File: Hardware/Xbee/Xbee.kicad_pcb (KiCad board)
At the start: 2 copper layers, 100 x 50 mm, 44 parts, among them J1 Alimentación, J2 Raspberry, J3 Pines 1, J4 Pines 2, J5 Programación, J6 Entrada, J7 Salida, K1 Rele12V, Q1 BC338, Q2 BC338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

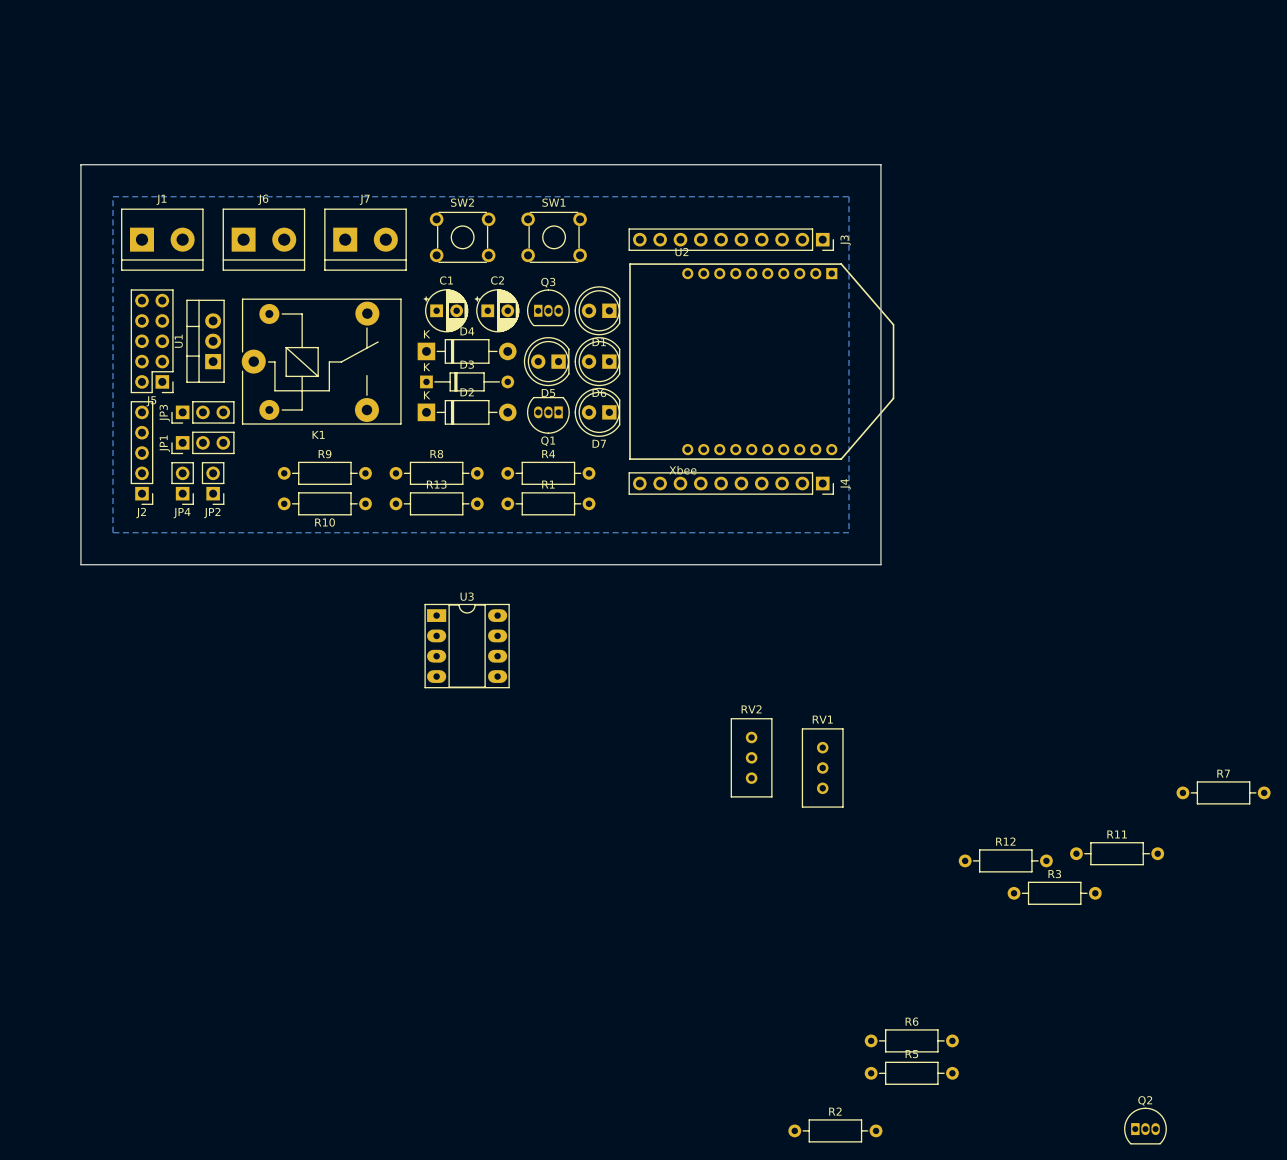
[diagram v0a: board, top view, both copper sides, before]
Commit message: PCB footprint placement
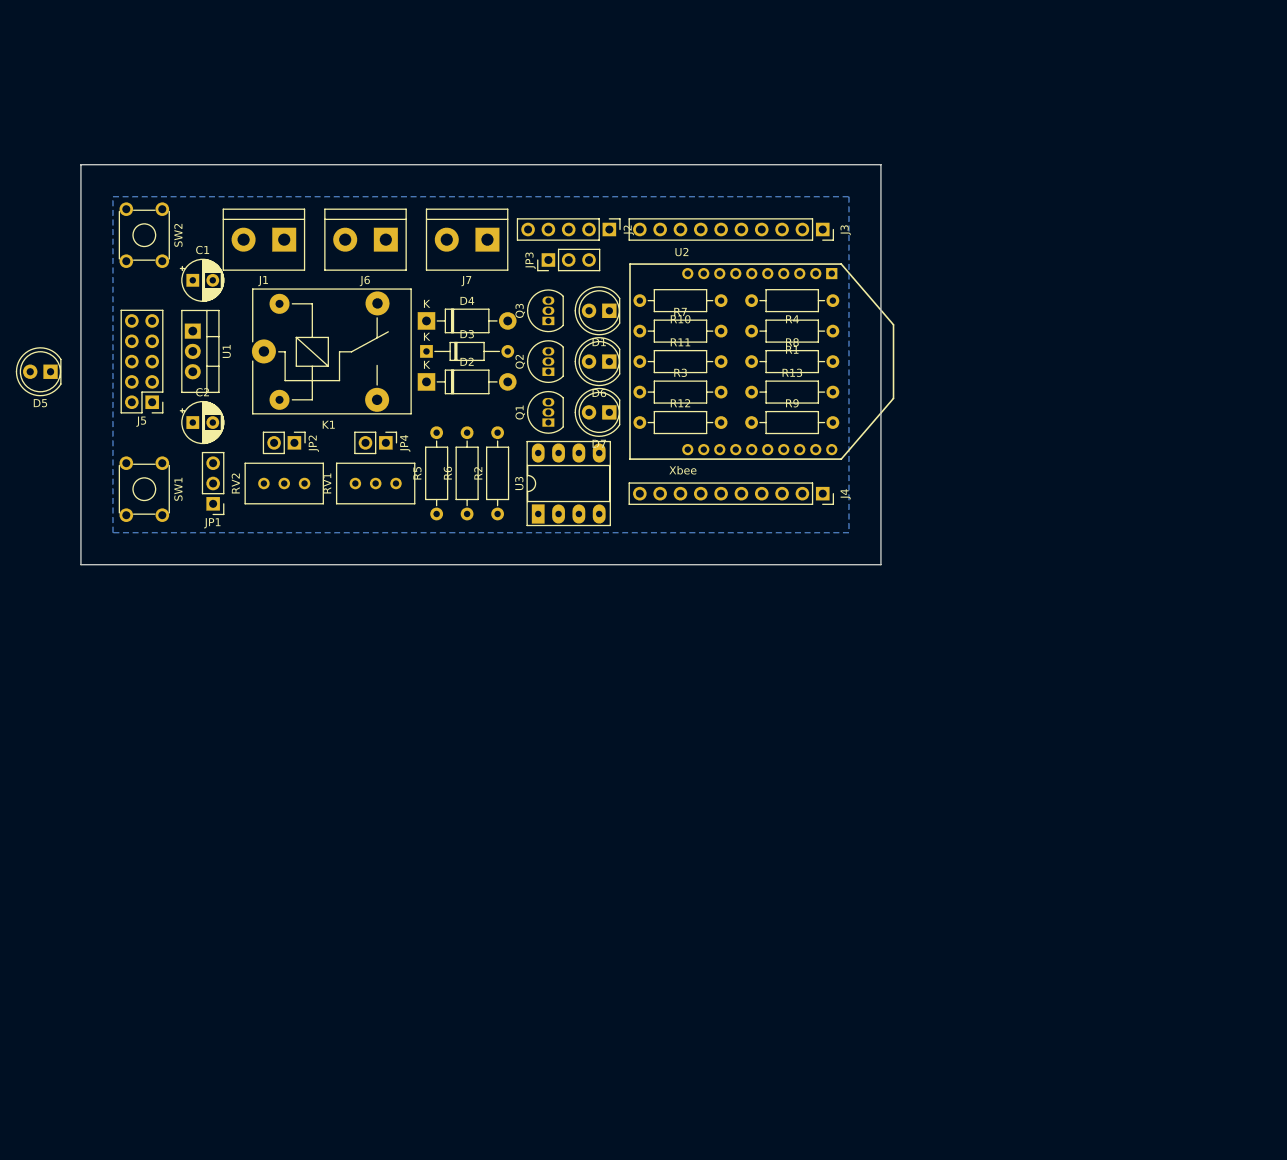
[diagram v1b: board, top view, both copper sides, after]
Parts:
- moved Q2 119.8 mm to (138.4, 55.9), turned to 90 degrees
- moved R7 89.1 mm to (149.9, 50.8)
- moved R5 88.5 mm to (124.5, 73.7), turned to 90 degrees
- moved R2 85.6 mm to (132.1, 73.7), turned to 90 degrees
- moved R6 83.0 mm to (128.3, 73.7), turned to 90 degrees
- moved R11 82.2 mm to (149.9, 54.6)
- moved R3 78.2 mm to (149.9, 58.4)
- moved RV2 68.7 mm to (102.9, 69.8), turned to 90 degrees
- moved R12 68.2 mm to (149.9, 62.2)
- moved J2 67.1 mm to (146.1, 38.1), turned to 270 degrees
- moved RV1 67.1 mm to (114.3, 69.8), turned to 90 degrees
- moved D5 63.5 mm to (76.2, 55.9)
- moved R9 58.8 mm to (163.8, 62.2)
- moved SW1 54.9 mm to (90.2, 67.3), turned to 270 degrees
- moved R10 51.2 mm to (160.0, 47.0)
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
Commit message: Started routing
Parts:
- added REF**: MountingHole_2.1mm, MountingHole:MountingHole_2.1mm, F.Cu at (177.5, 77.5)
- added REF**: MountingHole_2.1mm, MountingHole:MountingHole_2.1mm, F.Cu at (82.5, 77.5)
- added REF**: MountingHole_2.1mm, MountingHole:MountingHole_2.1mm, F.Cu at (177.5, 32.5)
- added REF**: MountingHole_2.1mm, MountingHole:MountingHole_2.1mm, F.Cu at (82.5, 32.5)
- D5, D6: footprint LED_THT:LED_D5.0mm -> Connector_PinSocket_2.54mm:PinSocket_1x02_P2.54mm_Vertical
- moved D5 63.6 mm to (138.4, 42.5), turned to 270 degrees
- moved JP3 41.1 mm to (106.7, 67.9), turned to 270 degrees
- moved D3 19.8 mm to (136.5, 67.9)
- moved U3 19.4 mm to (124.5, 59.1)
- moved RV2 15.3 mm to (118.1, 71.1), turned to 270 degrees
- moved R3 14.7 mm to (146.7, 72.4), turned to 180 degrees
- moved JP4 14.5 mm to (105.4, 71.8), turned to 90 degrees
- moved D4 13.3 mm to (123.2, 62.9)
- moved JP1 13.1 mm to (106.7, 64.1), turned to 270 degrees
- moved J7 12.7 mm to (118.1, 40.0)
- moved D6 12.1 mm to (146.1, 42.5), turned to 270 degrees
- moved J6 11.4 mm to (129.5, 40.0)
- moved JP2 10.3 mm to (99.1, 71.8), turned to 90 degrees
- moved D2 9.52 mm to (123.2, 47.6)
- moved SW2 9.25 mm to (87.6, 44.5), turned to 90 degrees
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- renumbered R4 to R1, R1 to R2, R2 to R3, R3 to R4
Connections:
- J6 pad 1: /Rasp.In -> GNDREF
- J6 pad 2: GNDREF -> /Rasp.In
- K1 pad 1: Net-(K1-Pad1) -> Net-(J7-Pad2)
- K1 pad 3: (no net) -> +12V
- K1 pad 4: (no net) -> Net-(K1-Pad4)
- K1 pad 5: (no net) -> +12V
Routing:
- net +12V: track 0.00 -> 59.0 mm, vias 0 -> 4
- net Net-(D4-Pad2): track 0.00 -> 44.2 mm, vias 0 -> 4
- net Net-(J7-Pad2): track 0.00 -> 23.5 mm, vias 0 -> 1
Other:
- board text added: "+"
- board text added: "-"

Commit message: Routing
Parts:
- C2: value 10u -> 1u
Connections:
- net /Rasp.In renamed /DIO2-Entrada
- net /Rasp.Out renamed /DIO2-Salida
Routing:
- net Net-(Q3-Pad2): track 0.00 -> 45.3 mm, vias 0 -> 2
- net Net-(JP4-Pad2): track 0.00 -> 30.8 mm, vias 0 -> 2
- net Net-(D4-Pad2): track 44.2 -> 62.1 mm, vias 4 -> 6
- net +3V3: track 0.00 -> 5.98 mm

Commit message: SMD components
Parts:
- removed D2: 1N4007, Diode_THT:D_DO-41_SOD81_P10.16mm_Horizontal
- removed R3: 330, Resistor_THT:R_Axial_DIN0207_L6.3mm_D2.5mm_P10.16mm_Horizontal
- removed R4: 560, Resistor_THT:R_Axial_DIN0207_L6.3mm_D2.5mm_P10.16mm_Horizontal
- removed REF** (x4): MountingHole_2.1mm, MountingHole:MountingHole_2.1mm
- D1, D7: footprint LED_THT:LED_D5.0mm -> LED_SMD:LED_0805_2012Metric
- U1: value LM317 -> AZ1117-3.3; footprint Package_TO_SOT_THT:TO-220-3_Vertical -> Package_TO_SOT_SMD:SOT-223-3_TabPin2
- U3: footprint Package_DIP:DIP-8_W7.62mm_Socket_LongPads -> Package_SO:SO-8_3.9x4.9mm_P1.27mm
- moved U3 6.45 mm to (128.3, 53.8)
- moved D7 4.10 mm to (144.5, 55.9)
- moved U1 3.07 mm to (96.5, 54.9), turned to 0 degrees
- moved D1 1.98 mm to (144.5, 52.1)
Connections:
- U1 pad 1: Net-(R3-Pad2) -> GNDREF

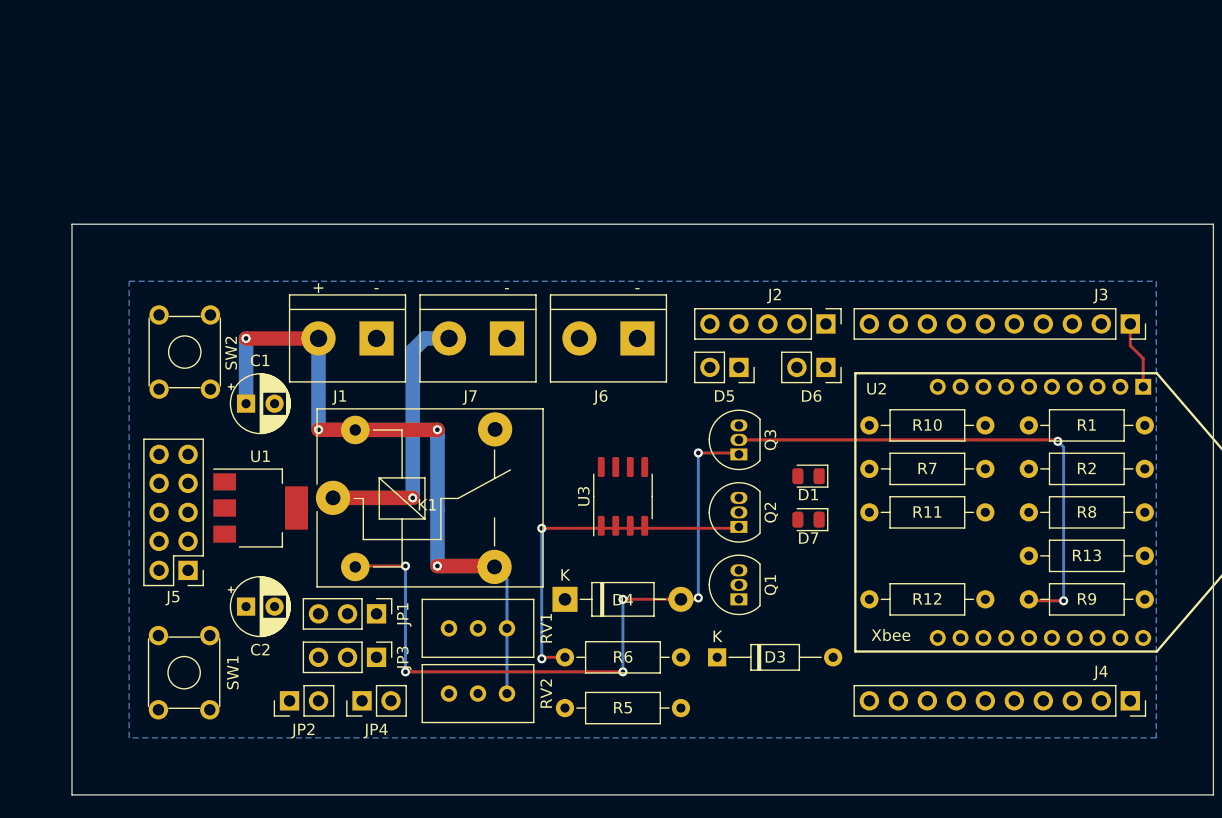
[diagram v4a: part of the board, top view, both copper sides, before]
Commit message: MOSFET, R SMD
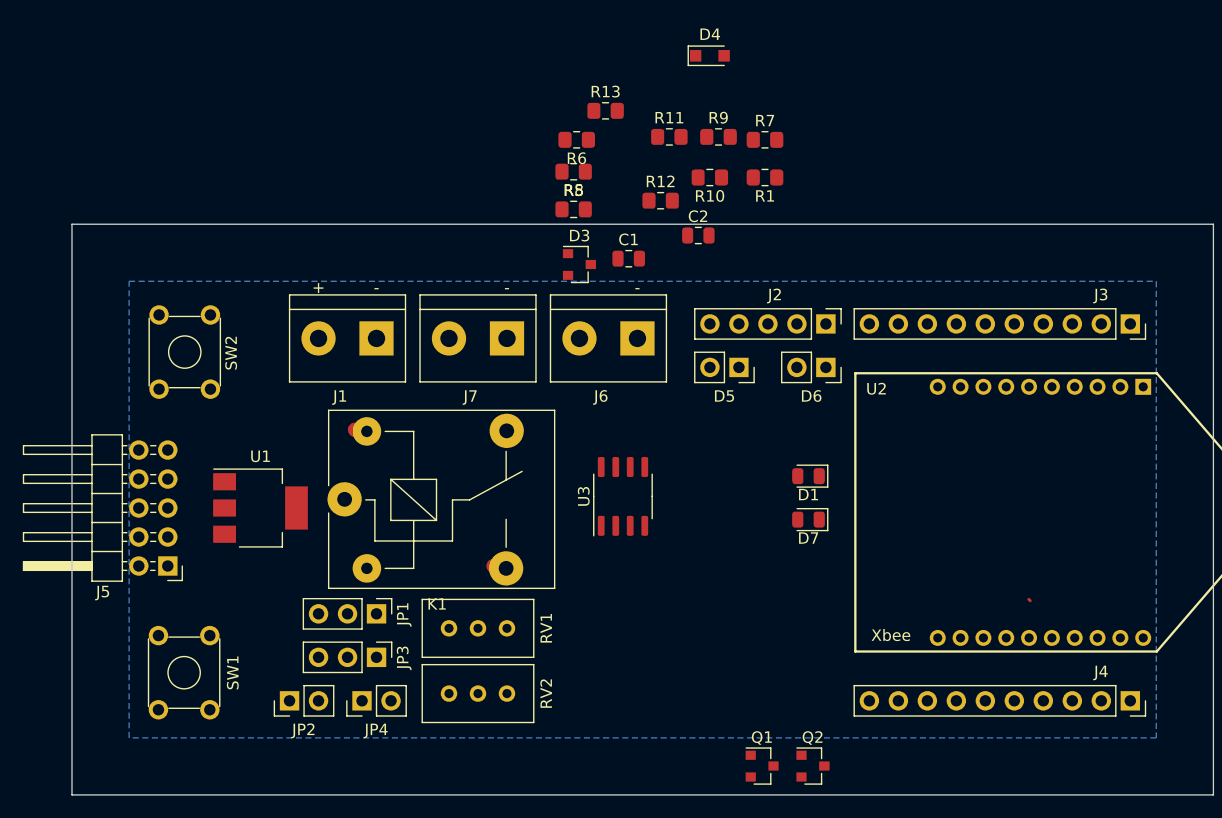
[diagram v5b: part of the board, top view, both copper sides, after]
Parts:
- removed Q3: BC338, Package_TO_SOT_THT:TO-92_Inline
- removed R2: 68, Resistor_THT:R_Axial_DIN0207_L6.3mm_D2.5mm_P10.16mm_Horizontal
- C1, C2: footprint Capacitor_THT:CP_Radial_D5.0mm_P2.50mm -> Capacitor_SMD:C_0805_2012Metric
- D1: value Assoc-RSSI -> Blue Assoc-RSSI
- D3: footprint Diode_THT:D_DO-35_SOD27_P10.16mm_Horizontal -> Diode_SMD:D_SOT-23_ANK
- D4: value 1N4007 -> 1N4007WS; footprint Diode_THT:D_DO-41_SOD81_P10.16mm_Horizontal -> Diode_SMD:D_SOD-323_HandSoldering
- D7: value LED Salida -> LED Green Salida
- J5: footprint Connector_PinHeader_2.54mm:PinHeader_2x05_P2.54mm_Vertical -> Connector_PinHeader_2.54mm:PinHeader_2x05_P2.54mm_Horizontal
- K1: value Rele12V -> SANYOU_SRD_Form_C
- Q1: value BC338 -> 2N7002; footprint Package_TO_SOT_THT:TO-92_Inline -> Package_TO_SOT_SMD:SOT-23
- Q2: value BC338 -> AP2300; footprint Package_TO_SOT_THT:TO-92_Inline -> Package_TO_SOT_SMD:SOT-23
- R1, R10, R11, R12, R6, R7, R8: footprint Resistor_THT:R_Axial_DIN0207_L6.3mm_D2.5mm_P10.16mm_Horizontal -> Resistor_SMD:R_0805_2012Metric_Pad1.15x1.40mm_HandSolder
- R13: value 680 -> 4k7; footprint Resistor_THT:R_Axial_DIN0207_L6.3mm_D2.5mm_P10.16mm_Horizontal -> Resistor_SMD:R_0805_2012Metric_Pad1.15x1.40mm_HandSolder
- R5, R9: value 10k -> 330; footprint Resistor_THT:R_Axial_DIN0207_L6.3mm_D2.5mm_P10.16mm_Horizontal -> Resistor_SMD:R_0805_2012Metric_Pad1.15x1.40mm_HandSolder
- moved R13 53.8 mm to (126.7, 20.1)
- moved C2 51.3 mm to (134.9, 31.0)
- moved D4 49.3 mm to (135.9, 15.2)
- moved R9 48.8 mm to (136.6, 22.4)
- moved R5 47.9 mm to (124.0, 25.4)
- moved R8 47.9 mm to (124.0, 28.7)
- moved R6 46.3 mm to (124.2, 22.6)
- moved R1 39.7 mm to (140.7, 25.9)
- moved R12 39.4 mm to (131.6, 27.9)
- moved R11 37.3 mm to (132.3, 22.4)
- moved D3 36.5 mm to (124.5, 33.5)
- moved C1 35.9 mm to (128.8, 33.0)
- moved R10 32.5 mm to (135.9, 25.9)
- moved R7 30.2 mm to (140.7, 22.6)
- moved Q2 21.9 mm to (144.9, 77.5), turned to 0 degrees
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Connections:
- Q1 pad 1: +3V3 -> Net-(Q1-Pad1)
- Q1 pad 2: Net-(Q1-Pad2) -> GNDREF
- Q1 pad 3: Net-(Q1-Pad3) -> Net-(JP4-Pad2)
- Q2 pad 1: Net-(JP4-Pad2) -> Net-(Q2-Pad1)
- Q2 pad 2: Net-(Q2-Pad2) -> GNDREF
- Q2 pad 3: GNDREF -> Net-(D4-Pad2)
- R1 pad 1: Net-(Q1-Pad2) -> Net-(D1-Pad2)
- R5 pad 2: Net-(Q2-Pad2) -> Net-(Q1-Pad1)
- R9 pad 1: Net-(Q3-Pad2) -> Net-(Q2-Pad1)
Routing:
- net Net-(D4-Pad2): track 62.1 -> 0.11 mm, vias 6 -> 0
- net +12V: track 59.0 -> 1.68 mm, vias 4 -> 0
- net Net-(Q3-Pad2): track 45.3 -> 0.00 mm, vias 2 -> 0
- net Net-(JP4-Pad2): track 30.8 -> 0.00 mm, vias 2 -> 0
- net Net-(J7-Pad2): track 23.5 -> 0.00 mm, vias 1 -> 0
- net +3V3: track 5.98 -> 0.00 mm

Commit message: Sheets-Text
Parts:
- moved C2 36.7 mm to (140.7, 67.2)
- moved C1 33.4 mm to (140.7, 64.3)
- moved U1 0.92 mm to (96.0, 54.1)
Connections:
- net Net-(D4-Pad2) renamed /Bobina
- net Net-(J7-Pad2) renamed /Salida-Rele
- net Net-(JP1-Pad2) renamed /LED-Assoc-RSSI
- net Net-(JP4-Pad2) renamed /Bat-DIO4

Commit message: Battery Charger
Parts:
- added J8: Batería, TerminalBlock:TerminalBlock_bornier-2_P5.08mm, F.Cu at (95.2, 17.5)
- added Q3: DMP3013SFV, Package_TO_SOT_SMD:SOT-23, F.Cu at (117.9, 17.3)
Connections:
- J1 pad 2: +12V -> /Vin+
- R11 pad 2: Net-(R11-Pad2) -> +12V
- U3 pad 1: Net-(R11-Pad2) -> /CargaBatería
